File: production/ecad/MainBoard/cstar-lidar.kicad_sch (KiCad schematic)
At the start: 1 part, among them J1 532610771

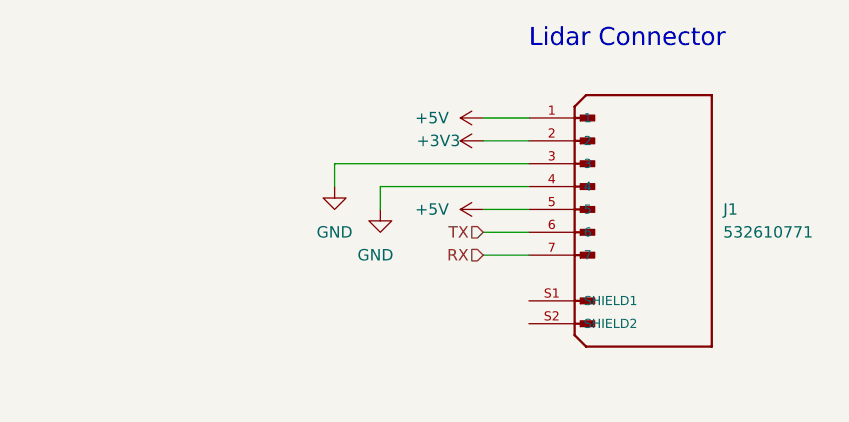
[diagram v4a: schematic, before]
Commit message: added global nets and grounded shield
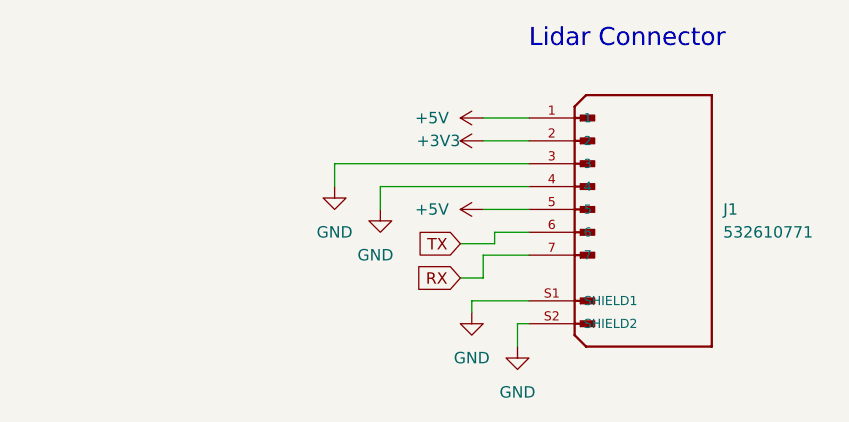
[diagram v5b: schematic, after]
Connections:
- net GND: now also J1.S1 (SHIELD1), J1.S2 (SHIELD2)
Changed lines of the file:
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@@
 (kicad_sch (version 20230121) (generator eeschema)
   (paper "A4")
+  (wire (pts (xy 133.35 83.82) (xy 133.35 86.36))
+    (stroke (width 0) (type default))
+  )
   (wire (pts (xy 113.03 66.04) (xy 134.62 66.04))
+    (stroke (width 0) (type default))
+  )
+  (wire (pts (xy 134.62 83.82) (xy 133.35 83.82))
     (stroke (width 0) (type default))
   )
@@
     (stroke (width 0) (type default))
   )
+  (wire (pts (xy 134.62 81.28) (xy 128.27 81.28))
+    (stroke (width 0) (type default))
+  )
   (wire (pts (xy 129.54 63.5) (xy 134.62 63.5))
     (stroke (width 0) (type default))
   )
-  (wire (pts (xy 129.54 73.66) (xy 134.62 73.66))
+  (wire (pts (xy 128.27 81.28) (xy 128.27 82.55))
+    (stroke (width 0) (type default))
+  )
+  (wire (pts (xy 127 74.93) (xy 130.81 74.93))
+    (stroke (width 0) (type default))
+  )
+  (wire (pts (xy 129.54 78.74) (xy 129.54 76.2))
+    (stroke (width 0) (type default))
+  )
+  (wire (pts (xy 130.81 74.93) (xy 130.81 73.66))
     (stroke (width 0) (type default))
   )
@@
     (stroke (width 0) (type default))
   )
+  (wire (pts (xy 129.54 76.2) (xy 134.62 76.2))
+    (stroke (width 0) (type default))
+  )
   (wire (pts (xy 113.03 66.04) (xy 113.03 68.58))
     (stroke (width 0) (type default))
@@
     (stroke (width 0) (type default))
   )
-  (wire (pts (xy 129.54 76.2) (xy 134.62 76.2))
+  (wire (pts (xy 127 78.74) (xy 129.54 78.74))
+    (stroke (width 0) (type default))
+  )
+  (wire (pts (xy 130.81 73.66) (xy 134.62 73.66))
     (stroke (width 0) (type default))
   )
@@
     (effects (font (size 2 2)) (justify left bottom))
   )
-  (hierarchical_label "RX" (shape input) (at 129.54 76.2 180) (fields_autoplaced)
+  (global_label "RX" (shape input) (at 127 78.74 180) (fields_autoplaced)
     (effects (font (size 1.27 1.27)) (justify right))
+    (property "Intersheetrefs" "${INTERSHEET_REFS}" (at 121.5353 78.74 0)
+      (effects (font (size 1.27 1.27)) (justify right) hide)
+    )
   )
-  (hierarchical_label "TX" (shape input) (at 129.54 73.66 180) (fields_autoplaced)
+  (global_label "TX" (shape input) (at 127 74.93 180) (fields_autoplaced)
     (effects (font (size 1.27 1.27)) (justify right))
+    (property "Intersheetrefs" "${INTERSHEET_REFS}" (at 121.8377 74.93 0)
+      (effects (font (size 1.27 1.27)) (justify right) hide)
+    )
+  )
+  (symbol (lib_id "power:GND") (at 133.35 86.36 0) (unit 1)
+    (in_bom yes) (on_board yes) (dnp no) (fields_autoplaced)
+    (property "Reference" "#PWR06" (at 133.35 92.71 0)
+      (effects (font (size 1.27 1.27)) hide)
+    )
+    (property "Value" "GND" (at 133.35 91.44 0)
+      (effects (font (size 1.27 1.27)))
+    )
+    (property "Footprint" "" (at 133.35 86.36 0)
+      (effects (font (size 1.27 1.27)) hide)
+    )
+    (property "Datasheet" "" (at 133.35 86.36 0)
+      (effects (font (size 1.27 1.27)) hide)
+    )
+    (pin "1")
+    (instances
+      (project "cstar-lidar"
+        (path "/f4254b98-3297-4812-862b-6470cd23e6be"
+          (reference "#PWR06") (unit 1)
+        )
+      )
+    )
   )
   (symbol (lib_id "power:GND") (at 118.11 71.12 0) (unit 1)
@@
         )
       )
+    )
+  )
+  (symbol (lib_id "power:GND") (at 128.27 82.55 0) (unit 1)
+    (in_bom yes) (on_board yes) (dnp no) (fields_autoplaced)
+    (property "Reference" "#PWR07" (at 128.27 88.9 0)
+      (effects (font (size 1.27 1.27)) hide)
+    )
+    (property "Value" "GND" (at 128.27 87.63 0)
+      (effects (font (size 1.27 1.27)))
+    )
+    (property "Footprint" "" (at 128.27 82.55 0)
+      (effects (font (size 1.27 1.27)) hide)
+    )
+    (property "Datasheet" "" (at 128.27 82.55 0)
+      (effects (font (size 1.27 1.27)) hide)
+    )
+    (pin "1")
+    (instances
+      (project "cstar-lidar"
+        (path "/f4254b98-3297-4812-862b-6470cd23e6be"
+          (reference "#PWR07") (unit 1)
+        )
+      )

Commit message: changed names of global connections
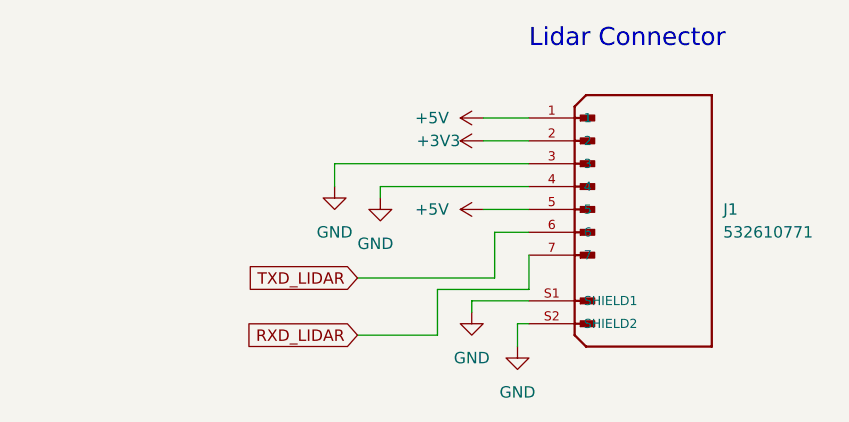
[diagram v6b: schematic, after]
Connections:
- net RX renamed RXD_LIDAR
- net TX renamed TXD_LIDAR
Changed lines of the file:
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@@
+    (stroke (width 0) (type default))
+  )
+  (wire (pts (xy 134.62 80.01) (xy 134.62 76.2))
     (stroke (width 0) (type default))
   )
@@
     (stroke (width 0) (type default))
   )
-  (wire (pts (xy 127 74.93) (xy 130.81 74.93))
+  (wire (pts (xy 115.57 78.74) (xy 130.81 78.74))
     (stroke (width 0) (type default))
   )
-  (wire (pts (xy 129.54 78.74) (xy 129.54 76.2))
+  (wire (pts (xy 124.46 85.09) (xy 124.46 80.01))
     (stroke (width 0) (type default))
   )
-  (wire (pts (xy 130.81 74.93) (xy 130.81 73.66))
+  (wire (pts (xy 130.81 78.74) (xy 130.81 73.66))
     (stroke (width 0) (type default))
   )
-  (wire (pts (xy 118.11 68.58) (xy 118.11 71.12))
+  (wire (pts (xy 118.11 68.58) (xy 118.11 69.85))
     (stroke (width 0) (type default))
   )
@@
     (stroke (width 0) (type default))
   )
-  (wire (pts (xy 129.54 76.2) (xy 134.62 76.2))
+  (wire (pts (xy 124.46 80.01) (xy 134.62 80.01))
     (stroke (width 0) (type default))
   )
@@
     (stroke (width 0) (type default))
   )
-  (wire (pts (xy 127 78.74) (xy 129.54 78.74))
+  (wire (pts (xy 115.57 85.09) (xy 124.46 85.09))
     (stroke (width 0) (type default))
   )
@@
     (effects (font (size 2 2)) (justify left bottom))
   )
-  (global_label "RX" (shape input) (at 127 78.74 180) (fields_autoplaced)
+  (global_label "RXD_LIDAR" (shape input) (at 115.57 85.09 180) (fields_autoplaced)
     (effects (font (size 1.27 1.27)) (justify right))
-    (property "Intersheetrefs" "${INTERSHEET_REFS}" (at 121.5353 78.74 0)
+    (property "Intersheetrefs" "${INTERSHEET_REFS}" (at 102.6062 85.09 0)
       (effects (font (size 1.27 1.27)) (justify right) hide)
     )
   )
-  (global_label "TX" (shape input) (at 127 74.93 180) (fields_autoplaced)
+  (global_label "TXD_LIDAR" (shape input) (at 115.57 78.74 180) (fields_autoplaced)
     (effects (font (size 1.27 1.27)) (justify right))
-    (property "Intersheetrefs" "${INTERSHEET_REFS}" (at 121.8377 74.93 0)
+    (property "Intersheetrefs" "${INTERSHEET_REFS}" (at 102.9086 78.74 0)
       (effects (font (size 1.27 1.27)) (justify right) hide)
     )
@@
     )
   )
-  (symbol (lib_id "power:GND") (at 118.11 71.12 0) (unit 1)
+  (symbol (lib_id "power:GND") (at 118.11 69.85 0) (unit 1)
     (in_bom yes) (on_board yes) (dnp no)
-    (property "Reference" "#PWR04" (at 118.11 77.47 0)
+    (property "Reference" "#PWR04" (at 118.11 76.2 0)
       (effects (font (size 1.27 1.27)) hide)
     )
-    (property "Value" "GND" (at 115.57 76.2 0)
+    (property "Value" "GND" (at 115.57 74.93 0)
       (effects (font (size 1.27 1.27)) (justify left))
     )
-    (property "Footprint" "" (at 118.11 71.12 0)
+    (property "Footprint" "" (at 118.11 69.85 0)
       (effects (font (size 1.27 1.27)) hide)
     )
-    (property "Datasheet" "" (at 118.11 71.12 0)
+    (property "Datasheet" "" (at 118.11 69.85 0)
       (effects (font (size 1.27 1.27)) hide)
     )

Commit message: added jumpers
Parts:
- added J2, J3: Conn_01x02_Pin, symbol Connector:Conn_01x02_Pin
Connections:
- net RXD_LIDAR: now also J3.2 (Pin_2); no longer J1.7
- net TXD_LIDAR: now also J2.2 (Pin_2); no longer J1.6
- new net: J1.6, J2.1 (Pin_1)
- new net: J1.7, J3.1 (Pin_1)
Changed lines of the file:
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@@
+    (stroke (width 0) (type default))
+  )
+  (wire (pts (xy 92.71 78.74) (xy 99.06 78.74))
     (stroke (width 0) (type default))
   )
@@
     (stroke (width 0) (type default))
   )
+  (wire (pts (xy 102.87 85.09) (xy 124.46 85.09))
+    (stroke (width 0) (type default))
+  )
   (wire (pts (xy 128.27 81.28) (xy 128.27 82.55))
     (stroke (width 0) (type default))
   )
-  (wire (pts (xy 115.57 78.74) (xy 130.81 78.74))
-    (stroke (width 0) (type default))
-  )
   (wire (pts (xy 124.46 85.09) (xy 124.46 80.01))
     (stroke (width 0) (type default))
@@
     (stroke (width 0) (type default))
   )
+  (wire (pts (xy 101.6 78.74) (xy 130.81 78.74))
+    (stroke (width 0) (type default))
+  )
   (wire (pts (xy 118.11 68.58) (xy 134.62 68.58))
     (stroke (width 0) (type default))
@@
     (stroke (width 0) (type default))
   )
-  (wire (pts (xy 115.57 85.09) (xy 124.46 85.09))
+  (wire (pts (xy 92.71 85.09) (xy 100.33 85.09))
     (stroke (width 0) (type default))
   )
@@
     (effects (font (size 2 2)) (justify left bottom))
   )
-  (global_label "RXD_LIDAR" (shape input) (at 115.57 85.09 180) (fields_autoplaced)
+  (global_label "RXD_LIDAR" (shape input) (at 92.71 85.09 180) (fields_autoplaced)
     (effects (font (size 1.27 1.27)) (justify right))
-    (property "Intersheetrefs" "${INTERSHEET_REFS}" (at 102.6062 85.09 0)
+    (property "Intersheetrefs" "${INTERSHEET_REFS}" (at 79.7462 85.09 0)
       (effects (font (size 1.27 1.27)) (justify right) hide)
     )
   )
-  (global_label "TXD_LIDAR" (shape input) (at 115.57 78.74 180) (fields_autoplaced)
+  (global_label "TXD_LIDAR" (shape input) (at 92.71 78.74 180) (fields_autoplaced)
     (effects (font (size 1.27 1.27)) (justify right))
-    (property "Intersheetrefs" "${INTERSHEET_REFS}" (at 102.9086 78.74 0)
+    (property "Intersheetrefs" "${INTERSHEET_REFS}" (at 80.0486 78.74 0)
       (effects (font (size 1.27 1.27)) (justify right) hide)
     )
@@
         )
       )
+    )
+  )
+  (symbol (lib_id "Connector:Conn_01x02_Pin") (at 101.6 73.66 270) (unit 1)
+    (in_bom yes) (on_board yes) (dnp no)
+    (property "Reference" "J2" (at 93.98 68.58 90)
+      (effects (font (size 1.27 1.27)) (justify left))
+    )
+    (property "Value" "Conn_01x02_Pin" (at 93.98 71.12 90)
+      (effects (font (size 1.27 1.27)) (justify left))
+    )
+    (property "Footprint" "" (at 101.6 73.66 0)
+      (effects (font (size 1.27 1.27)) hide)
+    )
+    (property "Datasheet" "~" (at 101.6 73.66 0)
+      (effects (font (size 1.27 1.27)) hide)
+    )
+    (pin "1")
+    (pin "2")
+    (instances
+      (project "cstar-lidar"
+        (path "/f4254b98-3297-4812-862b-6470cd23e6be"
+          (reference "J2") (unit 1)
+        )
+      )
+    )
+  )
+  (symbol (lib_id "Connector:Conn_01x02_Pin") (at 102.87 80.01 270) (unit 1)
+    (in_bom yes) (on_board yes) (dnp no)
+    (property "Reference" "J3" (at 96.52 87.63 90)
+      (effects (font (size 1.27 1.27)) (justify left))
+    )
+    (property "Value" "Conn_01x02_Pin" (at 96.52 90.17 90)
+      (effects (font (size 1.27 1.27)) (justify left))
+    )
+    (property "Footprint" "" (at 102.87 80.01 0)
+      (effects (font (size 1.27 1.27)) hide)
+    )
+    (property "Datasheet" "~" (at 102.87 80.01 0)
+      (effects (font (size 1.27 1.27)) hide)
+    )
+    (pin "1")
+    (pin "2")
+    (instances
+      (project "cstar-lidar"
+        (path "/f4254b98-3297-4812-862b-6470cd23e6be"
+          (reference "J3") (unit 1)
+        )
+      )

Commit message: Lidar footprints added (0805 connector pins)
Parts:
- J2, J3: footprint (none) -> Connector_Phoenix_SPT:PhoenixContact_SPT_1.5_9-H-3.5_1x09_P3.5mm_Horizontal
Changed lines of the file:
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@@
       (effects (font (size 1.27 1.27)) (justify left))
     )
-    (property "Footprint" "" (at 101.6 73.66 0)
+    (property "Footprint" "Connector_Phoenix_SPT:PhoenixContact_SPT_1.5_9-H-3.5_1x09_P3.5mm_Horizontal" (at 101.6 73.66 0)
       (effects (font (size 1.27 1.27)) hide)
     )
@@
       (effects (font (size 1.27 1.27)) (justify left))
     )
-    (property "Footprint" "" (at 102.87 80.01 0)
+    (property "Footprint" "Connector_Phoenix_SPT:PhoenixContact_SPT_1.5_9-H-3.5_1x09_P3.5mm_Horizontal" (at 102.87 80.01 0)
       (effects (font (size 1.27 1.27)) hide)
     )
